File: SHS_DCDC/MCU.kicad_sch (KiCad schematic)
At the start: 15 parts, among them J3 Conn_ARM_JTAG_SWD_10, J4 Conn_01x02_Male, U6 ESP32-S2-MINI-1, U8 MIC5501-3.0YM5, Y1 2-SMD no lead

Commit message: 3D rendering progress
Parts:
- removed S1: TS02-66-70-BK-160-LCR-D, SW_TS02-66-70-BK-160-LCR-D, symbol SHS_DCDC:TS02-66-70-BK-160-LCR-D
- added SW1: TACT_SW, SHS_DCDC:ESWITCH_TL1105, symbol SHS_DCDC:TACT_SW
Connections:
- net GND: now also SW1.2
- net MCU_RST: now also SW1.1
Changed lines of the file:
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@@
 (kicad_sch (version 20211123) (generator eeschema)
   (paper "A4")
-  (junction (at 41.91 102.87) (diameter 0) (color 0 0 0 0)
-  )
   (junction (at 259.08 80.01) (diameter 0) (color 0 0 0 0)
   )
@@
   (junction (at 66.04 143.51) (diameter 0) (color 0 0 0 0)
   )
-  (junction (at 58.42 102.87) (diameter 0) (color 0 0 0 0)
+  (junction (at 36.83 107.95) (diameter 0) (color 0 0 0 0)
+  )
+  (junction (at 48.26 87.63) (diameter 0) (color 0 0 0 0)
   )
   (junction (at 165.1 31.75) (diameter 0) (color 0 0 0 0)
@@
   (junction (at 105.41 127) (diameter 0) (color 0 0 0 0)
   )
-  (junction (at 74.93 87.63) (diameter 0) (color 0 0 0 0)
-  )
-  (junction (at 41.91 85.09) (diameter 0) (color 0 0 0 0)
-  )
   (junction (at 105.41 139.7) (diameter 0) (color 0 0 0 0)
   )
@@
     (stroke (width 0) (type default) (color 0 0 0 0))
   )
-  (wire (pts (xy 36.83 102.87) (xy 41.91 102.87))
-    (stroke (width 0) (type default) (color 0 0 0 0))
-  )
   (wire (pts (xy 259.08 80.01) (xy 259.08 66.04))
     (stroke (width 0) (type default) (color 0 0 0 0))
@@
     (stroke (width 0) (type default) (color 0 0 0 0))
   )
-  (wire (pts (xy 41.91 85.09) (xy 74.93 85.09))
-    (stroke (width 0) (type default) (color 0 0 0 0))
-  )
-  (wire (pts (xy 36.83 91.44) (xy 36.83 85.09))
+  (wire (pts (xy 36.83 91.44) (xy 36.83 87.63))
     (stroke (width 0) (type default) (color 0 0 0 0))
   )
@@
     (stroke (width 0) (type default) (color 0 0 0 0))
   )
+  (wire (pts (xy 36.83 107.95) (xy 36.83 111.76))
+    (stroke (width 0) (type default) (color 0 0 0 0))
+  )
   (wire (pts (xy 118.11 130.81) (xy 118.11 127))
     (stroke (width 0) (type default) (color 0 0 0 0))
   )
-  (wire (pts (xy 74.93 91.44) (xy 71.12 91.44))
-    (stroke (width 0) (type default) (color 0 0 0 0))
-  )
   (wire (pts (xy 118.11 127) (xy 105.41 127))
     (stroke (width 0) (type default) (color 0 0 0 0))
@@
     (stroke (width 0) (type default) (color 0 0 0 0))
   )
-  (wire (pts (xy 45.72 91.44) (xy 41.91 91.44))
-    (stroke (width 0) (type default) (color 0 0 0 0))
-  )
   (wire (pts (xy 215.9 80.01) (xy 259.08 80.01))
     (stroke (width 0) (type default) (color 0 0 0 0))
   )
+  (wire (pts (xy 48.26 87.63) (xy 99.06 87.63))
+    (stroke (width 0) (type default) (color 0 0 0 0))
+  )
   (wire (pts (xy 92.71 160.02) (xy 143.51 160.02))
     (stroke (width 0) (type default) (color 0 0 0 0))
@@
     (stroke (width 0) (type default) (color 0 0 0 0))
   )
-  (wire (pts (xy 74.93 99.06) (xy 74.93 102.87))
-    (stroke (width 0) (type default) (color 0 0 0 0))
-  )
   (wire (pts (xy 118.11 137.16) (xy 143.51 137.16))
     (stroke (width 0) (type default) (color 0 0 0 0))
@@
     (stroke (width 0) (type default) (color 0 0 0 0))
   )
-  (wire (pts (xy 41.91 102.87) (xy 41.91 99.06))
-    (stroke (width 0) (type default) (color 0 0 0 0))
-  )
   (wire (pts (xy 215.9 120.65) (xy 227.33 120.65))
     (stroke (width 0) (type default) (color 0 0 0 0))
@@
     (stroke (width 0) (type default) (color 0 0 0 0))
   )
-  (wire (pts (xy 36.83 85.09) (xy 41.91 85.09))
+  (wire (pts (xy 48.26 87.63) (xy 48.26 90.17))
+    (stroke (width 0) (type default) (color 0 0 0 0))
+  )
+  (wire (pts (xy 36.83 87.63) (xy 48.26 87.63))
     (stroke (width 0) (type default) (color 0 0 0 0))
   )
@@
     (stroke (width 0) (type default) (color 0 0 0 0))
   )
-  (wire (pts (xy 36.83 99.06) (xy 36.83 102.87))
-    (stroke (width 0) (type default) (color 0 0 0 0))
-  )
   (wire (pts (xy 143.51 149.86) (xy 92.71 149.86))
     (stroke (width 0) (type default) (color 0 0 0 0))
@@
     (stroke (width 0) (type default) (color 0 0 0 0))
   )
-  (wire (pts (xy 71.12 99.06) (xy 74.93 99.06))
-    (stroke (width 0) (type default) (color 0 0 0 0))
-  )
   (wire (pts (xy 246.38 25.4) (xy 246.38 22.86))
     (stroke (width 0) (type default) (color 0 0 0 0))
@@
     (stroke (width 0) (type default) (color 0 0 0 0))
   )
+  (wire (pts (xy 48.26 107.95) (xy 36.83 107.95))
+    (stroke (width 0) (type default) (color 0 0 0 0))
+  )
   (wire (pts (xy 215.9 135.89) (xy 227.33 135.89))
     (stroke (width 0) (type default) (color 0 0 0 0))
@@
     (stroke (width 0) (type default) (color 0 0 0 0))
   )
-  (wire (pts (xy 74.93 87.63) (xy 74.93 91.44))
-    (stroke (width 0) (type default) (color 0 0 0 0))
-  )
   (wire (pts (xy 215.9 82.55) (xy 245.11 82.55))
     (stroke (width 0) (type default) (color 0 0 0 0))
@@
     (stroke (width 0) (type default) (color 0 0 0 0))
   )
-  (wire (pts (xy 58.42 105.41) (xy 58.42 102.87))
+  (wire (pts (xy 36.83 99.06) (xy 36.83 107.95))
     (stroke (width 0) (type default) (color 0 0 0 0))
   )
@@
     (stroke (width 0) (type default) (color 0 0 0 0))
   )
-  (wire (pts (xy 74.93 85.09) (xy 74.93 87.63))
-    (stroke (width 0) (type default) (color 0 0 0 0))
-  )
-  (wire (pts (xy 58.42 102.87) (xy 74.93 102.87))
-    (stroke (width 0) (type default) (color 0 0 0 0))
-  )
-  (wire (pts (xy 41.91 99.06) (xy 45.72 99.06))
+  (wire (pts (xy 48.26 105.41) (xy 48.26 107.95))
     (stroke (width 0) (type default) (color 0 0 0 0))
   )
@@
     (stroke (width 0) (type default) (color 0 0 0 0))
   )
-  (wire (pts (xy 41.91 91.44) (xy 41.91 85.09))
-    (stroke (width 0) (type default) (color 0 0 0 0))
-  )
   (wire (pts (xy 246.38 55.88) (xy 246.38 62.23))
     (stroke (width 0) (type default) (color 0 0 0 0))
@@
   )
   (wire (pts (xy 66.04 143.51) (xy 58.42 143.51))
-    (stroke (width 0) (type default) (color 0 0 0 0))
-  )
-  (wire (pts (xy 74.93 87.63) (xy 99.06 87.63))
-    (stroke (width 0) (type default) (color 0 0 0 0))
-  )
-  (wire (pts (xy 41.91 102.87) (xy 58.42 102.87))
     (stroke (width 0) (type default) (color 0 0 0 0))
   )
@@
     (pin "9")
   )
-  (symbol (lib_id "SHS_DCDC:GND-power") (at 58.42 105.41 0) (unit 1)
-    (in_bom yes) (on_board yes)
-    (property "Reference" "#PWR0119" (id 0) (at 58.42 111.76 0)
-      (effects (font (size 1.27 1.27)) hide)
-    )
-    (property "Value" "GND-power" (id 1) (at 58.547 108.6612 90)
-      (effects (font (size 1.27 1.27)) (justify right))
-    )
-    (property "Footprint" "" (id 2) (at 58.42 105.41 0)
-      (effects (font (size 1.27 1.27)) hide)
-    )
-    (property "Datasheet" "" (id 3) (at 58.42 105.41 0)
+  (symbol (lib_id "SHS_DCDC:GND-power") (at 36.83 111.76 0) (unit 1)
+    (in_bom yes) (on_board yes)
+    (property "Reference" "#PWR0119" (id 0) (at 36.83 118.11 0)
+      (effects (font (size 1.27 1.27)) hide)
+    )
+    (property "Value" "GND-power" (id 1) (at 36.957 115.0112 90)
+      (effects (font (size 1.27 1.27)) (justify right))
+    )
+    (property "Footprint" "" (id 2) (at 36.83 111.76 0)
+      (effects (font (size 1.27 1.27)) hide)
+    )
+    (property "Datasheet" "" (id 3) (at 36.83 111.76 0)
       (effects (font (size 1.27 1.27)) hide)
     )
@@
     (pin "2")
   )
-  (symbol (lib_id "SHS_DCDC:TS02-66-70-BK-160-LCR-D") (at 58.42 95.25 0) (unit 1)
-    (in_bom yes) (on_board yes) (fields_autoplaced)
-    (property "Reference" "S1" (id 0) (at 58.42 86.36 0))
-    (property "Value" "TS02-66-70-BK-160-LCR-D" (id 1) (at 58.42 88.9 0))
-    (property "Footprint" "SW_TS02-66-70-BK-160-LCR-D" (id 2) (at 58.42 87.63 0)
-      (effects (font (size 1.27 1.27)) (justify bottom) hide)
-    )
-    (property "Datasheet" "" (id 3) (at 58.42 95.25 0)
-      (effects (font (size 1.27 1.27)) hide)
-    )
-    (property "MANUFACTURER" "CUI Devices" (id 4) (at 46.99 90.17 0)
-      (effects (font (size 1.27 1.27)) (justify bottom) hide)
-    )
-    (property "PARTREV" "1.0" (id 5) (at 58.42 95.25 0)
-      (effects (font (size 1.27 1.27)) (justify bottom) hide)
-    )
-    (property "STANDARD" "Manufacturer Recommendations" (id 6) (at 57.15 85.09 0)
-      (effects (font (size 1.27 1.27)) (justify bottom) hide)
-    )
-    (pin "1")
-    (pin "2")
-    (pin "3")
-    (pin "4")
-  )
   (symbol (lib_id "SHS_DCDC:GND-power") (at 179.07 53.34 0) (unit 1)
     (in_bom yes) (on_board yes)
@@
       (effects (font (size 1.27 1.27)) hide)
     )
+    (pin "1")
+    (pin "2")
+  )
+  (symbol (lib_id "SHS_DCDC:TACT_SW") (at 48.26 97.79 270) (unit 1)
+    (in_bom yes) (on_board yes) (fields_autoplaced)
+    (property "Reference" "SW1" (id 0) (at 50.8 96.5199 90)
+      (effects (font (size 1.27 1.27)) (justify left))
+    )
+    (property "Value" "TACT_SW" (id 1) (at 50.8 99.0599 90)
+      (effects (font (size 1.27 1.27)) (justify left))
+    )
+    (property "Footprint" "SHS_DCDC:ESWITCH_TL1105" (id 2) (at 48.26 97.79 0)
+      (effects (font (size 1.27 1.27)) hide)
+    )
+    (property "Datasheet" "~" (id 3) (at 48.26 97.79 0)
+      (effects (font (size 1.27 1.27)) hide)
+    )

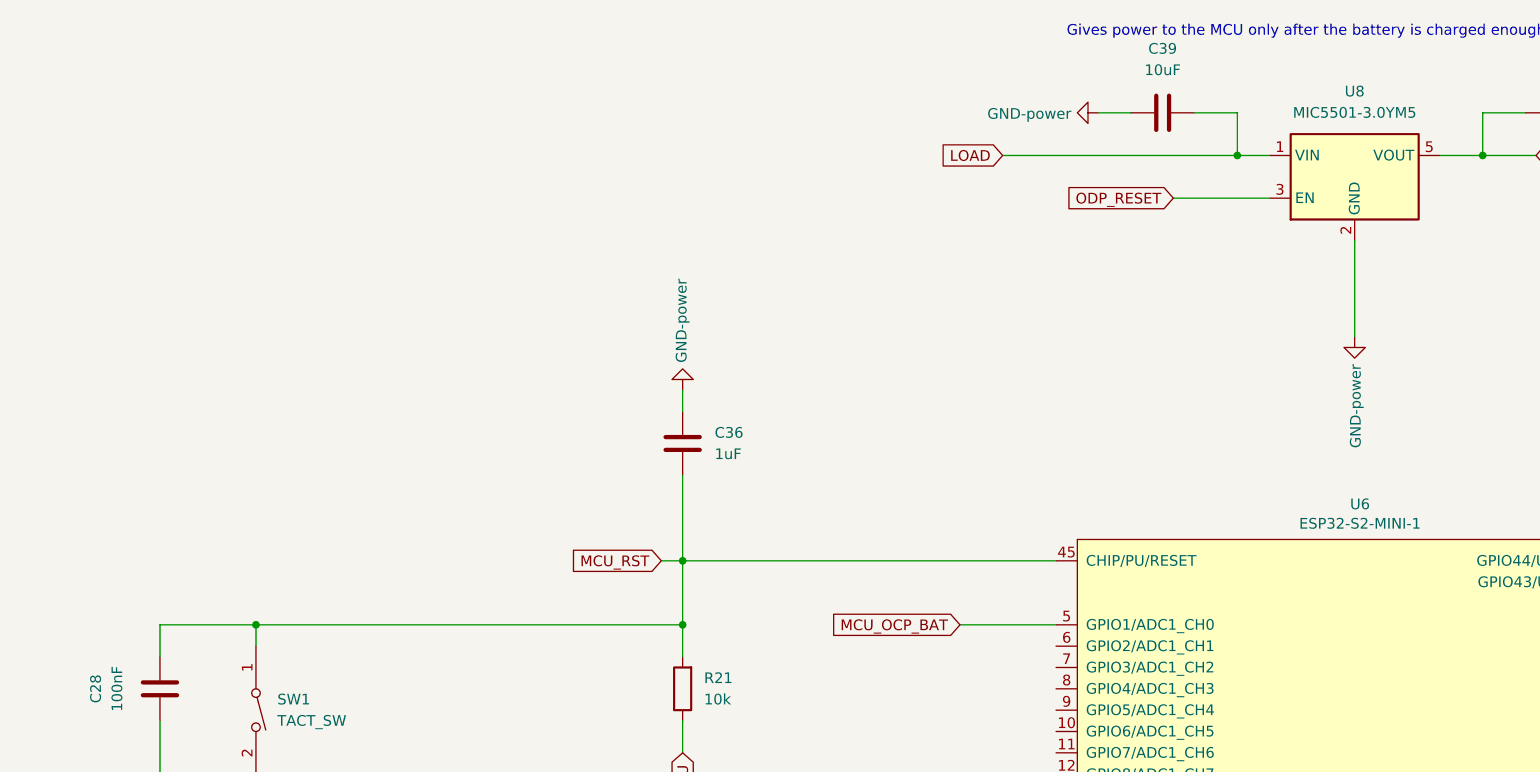
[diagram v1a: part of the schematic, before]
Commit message: 3D missing part
Many parts with no 3D view, have completed all of them
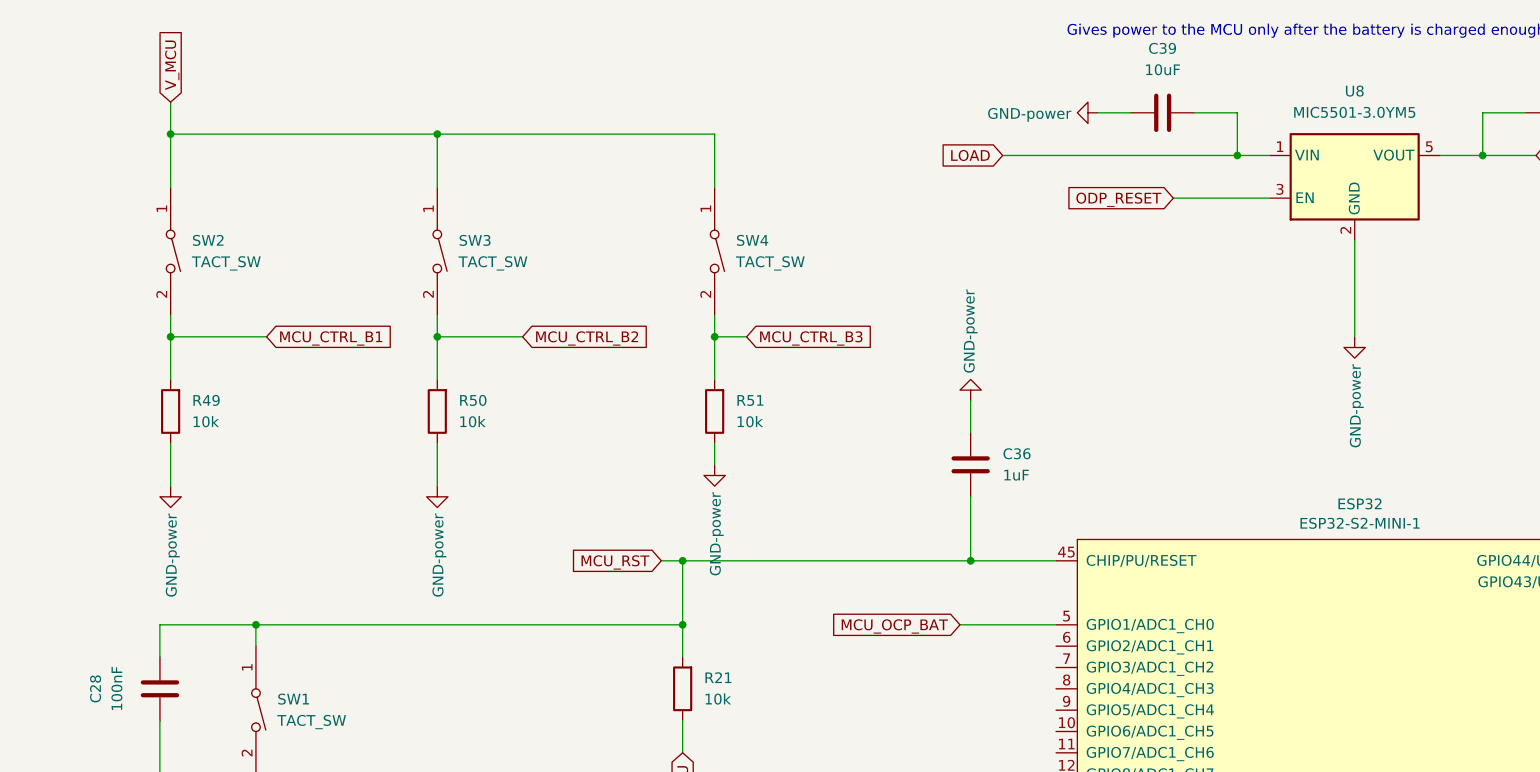
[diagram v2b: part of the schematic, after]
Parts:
- added R49, R50, R51: 10k, Resistor_SMD:R_0402_1005Metric, symbol Device:R
- added SW2, SW3, SW4: TACT_SW, SHS_DCDC:ESWITCH_TL1105, symbol SHS_DCDC:TACT_SW
- renumbered U6 to ESP32
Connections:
- net GND: now also R49.1, R50.1, R51.1
- net V_MCU: now also SW2.1, SW3.1, SW4.1
- new net MCU_CTRL_B1: R49.2, SW2.2
- new net MCU_CTRL_B2: R50.2, SW3.2
- new net MCU_CTRL_B3: R51.2, SW4.2
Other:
- moved on the sheet: C36

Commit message: DFU update
PCB update to setup 3 ways of FW/Debug capability:
1. JTAG (FW & Debug)
2. USB DFU (FW & Debug)
3. UART (FW only)
With BOOT0 button installed too
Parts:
- removed J4: Conn_01x02_Male, Connector_PinHeader_2.54mm:PinHeader_1x02_P2.54mm_Vertical, symbol Connector:Conn_01x02_Male
- added C41, C42: 100nF, Capacitor_SMD:C_0402_1005Metric, symbol Device:C
- added J4: 0022232041, digikey-kicad-library-master:PinHeader_1x4_P2.54mm_Drill1.02mm, symbol dk_Rectangular-Connectors-Headers-Male-Pins:0022232041
- added J5: 640456-2, digikey-footprints:PinHeader_1x2_P2.54mm_Drill1.02mm, symbol dk_Rectangular-Connectors-Headers-Male-Pins:640456-2
- added S1: PTS645SM43SMTR92_LFS, digikey-footprints:Switch_Tactile_SMD_6x6mm_PTS645, symbol dk_Tactile-Switches:PTS645SM43SMTR92_LFS
- C29: value 10uF -> 22uF
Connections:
- net GND: now also C41.1, C42.1, J4.4, S1.3, S1.4
- net MCU_ADC_IBAT: now also ESP32.16 (GPIO12/ADC2_CH1)
- net MCU_RX: now also J4.1
- net MCU_TX: now also J4.2
- net USB_D+: now also J5.2
- net USB_D-: now also J5.1
- net V_MCU: now also C42.2, J4.3
- net MCU_LMV324_VDD: now reaches ESP32.18 (GPIO14/ADC2_CH3)
- net MCU_INA181_VDD: now reaches ESP32.22 (ADC2_CH6/DAC_1/GPIO18)
- net MCU_L1_ONOFFSIG: now reaches ESP32.28 (GPIO33)
- net at ESP32.4 (GPIO0/BOOT): now also C41.2, S1.1, S1.2
- net MCU_ADC_BAT_CTRL: now reaches ESP32.9 (GPIO5/ADC1_CH4)
- net MCU_BL1_ONOFFSIG renamed MCU_L2_ONOFFSIG
- net MCU_BL2_ONOFFSIG renamed MCU_L3_ONOFFSIG
- net MCU_PWM_BL1 renamed MCU_PWM_L2
- net MCU_PWM_BL2 renamed MCU_PWM_L3
- net MCU_PWM_TL renamed MCU_PWM_L1
- net MCU_TL_ONOFFSIG renamed MCU_ADC_PV_CTRL
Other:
- note added: "USB_DFU"
- moved on the sheet: C2, C28, C29, C36, C37, C39, C40, ESP32, R21, R28, SW1, U8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
